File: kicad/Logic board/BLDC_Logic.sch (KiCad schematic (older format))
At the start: 21 parts

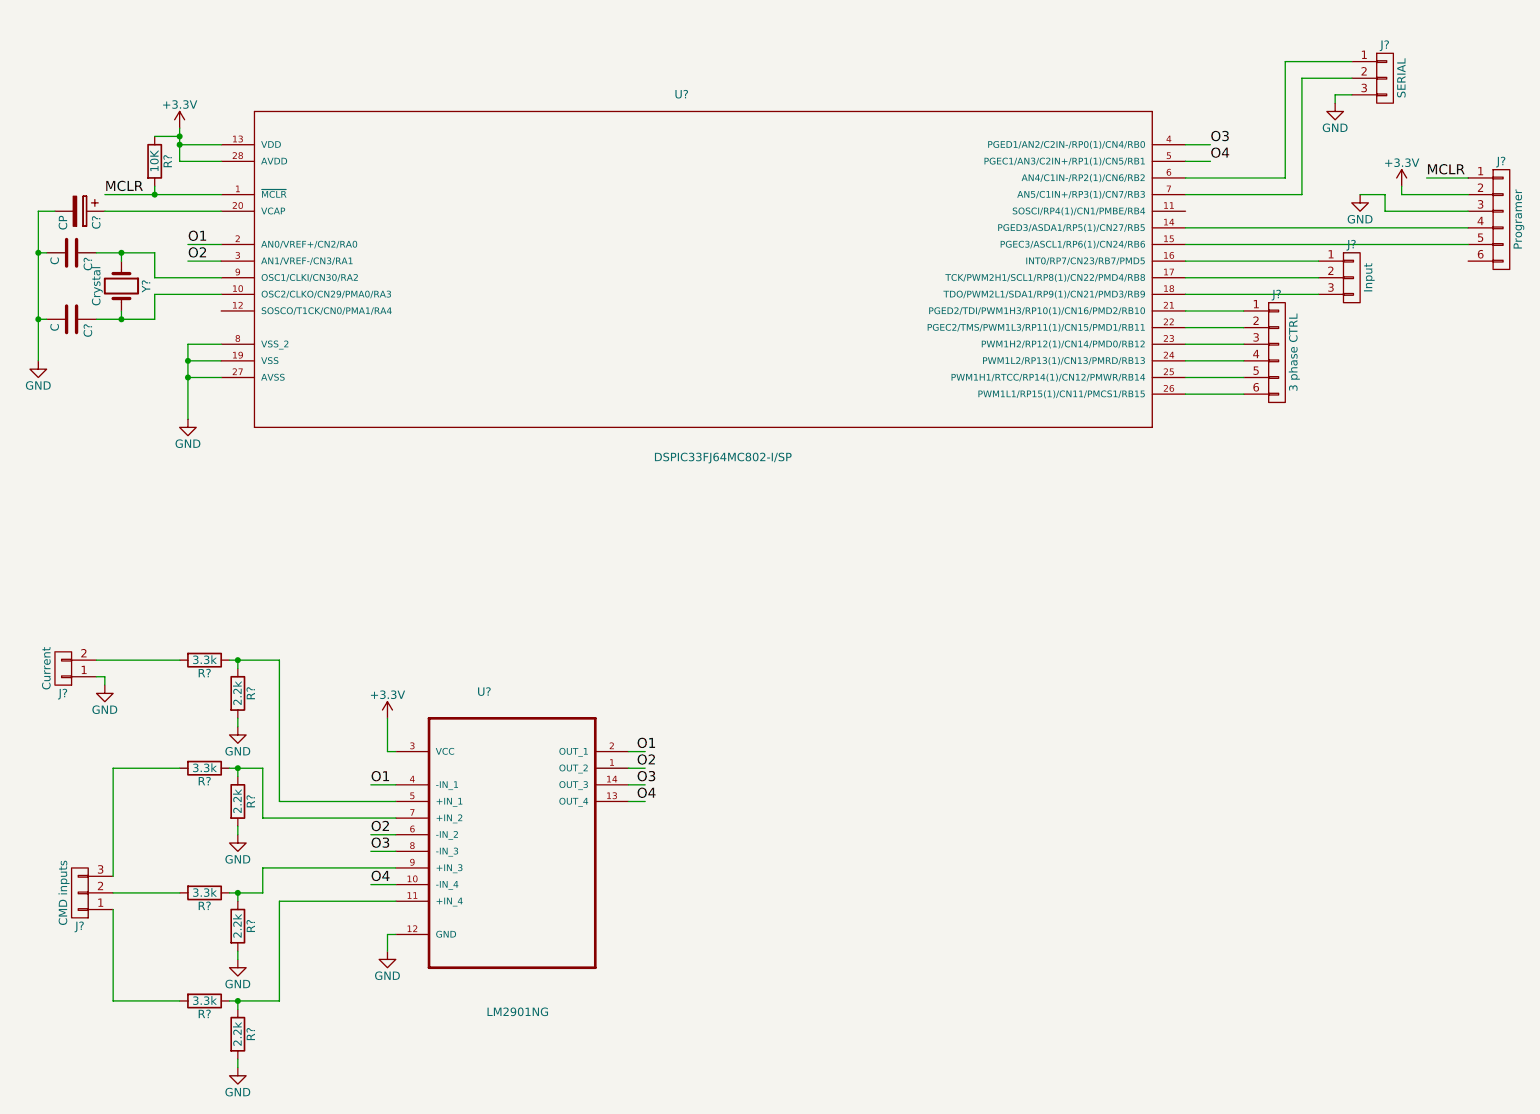
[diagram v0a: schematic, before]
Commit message: added MCLR Circuit
added MCLR circuit based on version 1 board
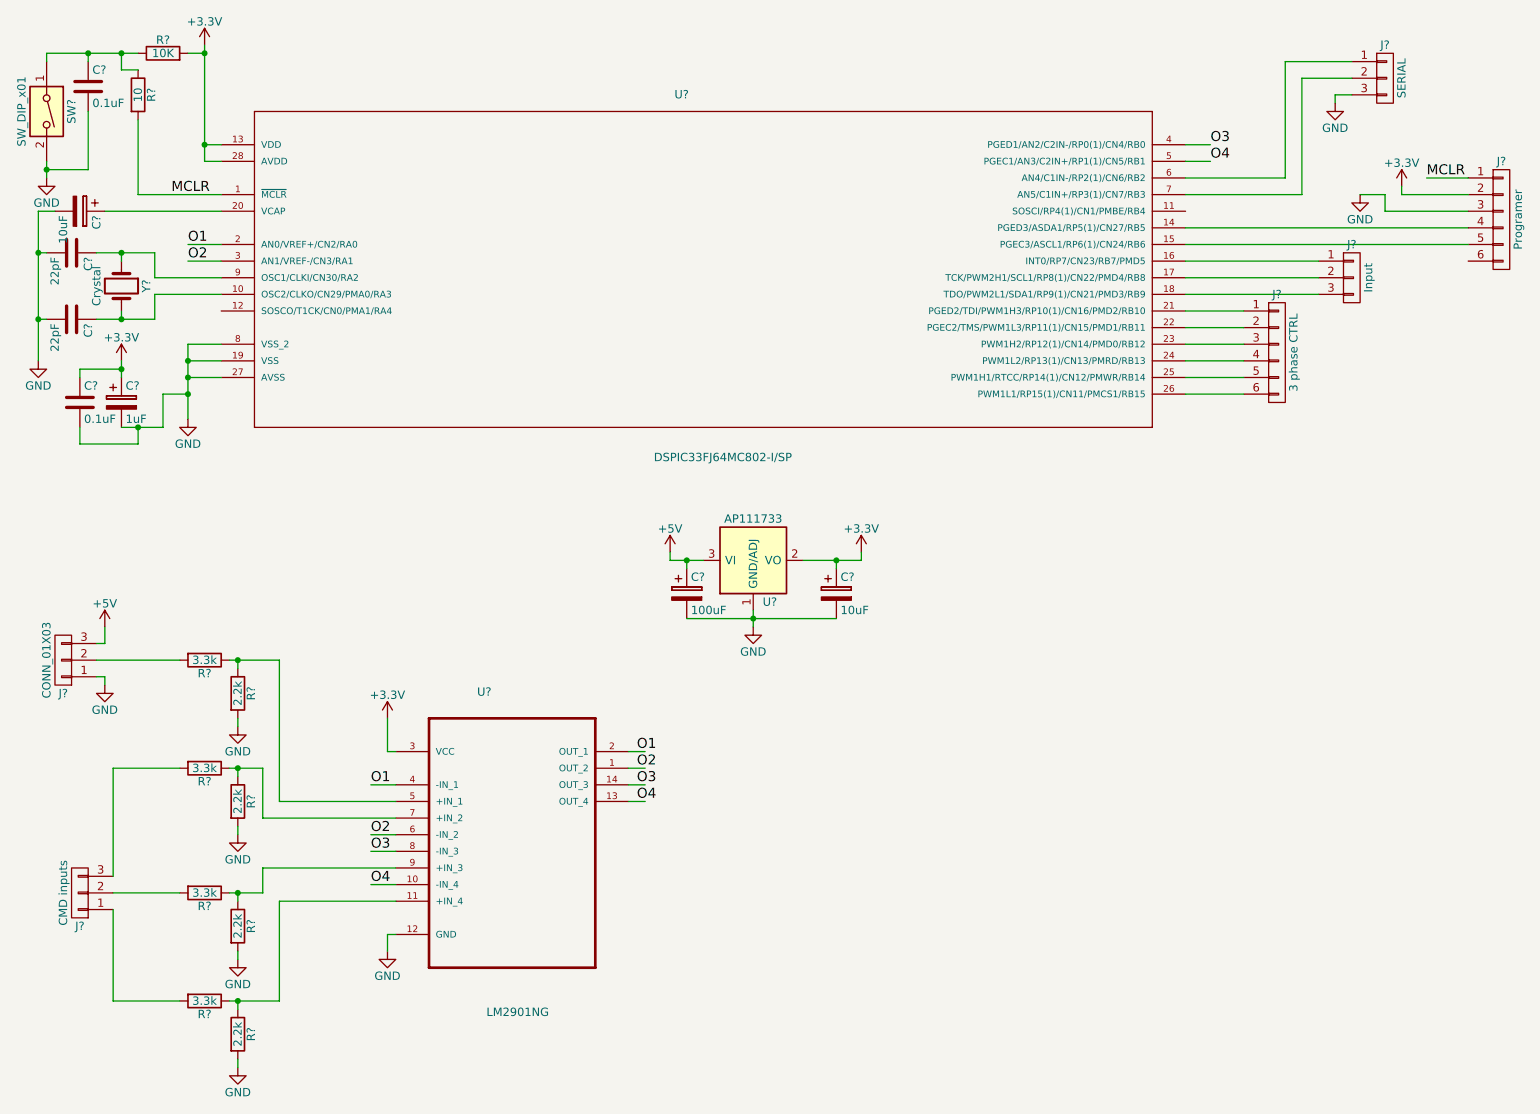
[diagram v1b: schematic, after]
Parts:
- removed J?: Current, symbol CONN_01X02
- added C?: 100uF, symbol CP
- added C?: 10uF, symbol CP
- added C?: 1uF, symbol CP
- added C? (x2): 0.1uF, symbol C
- added J?: CONN_01X03, symbol CONN_01X03
- added R?: 10, symbol R
- added SW?: SW_DIP_x01, symbol SW_DIP_x01
- added U?: AP111733, TO_SOT_Packages_SMD:SOT-223, symbol AP111733
- C?: value CP -> 10uF
- C? (x2): value C -> 22pF
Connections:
- net labels added: +5V
- wire segments 92 -> 119
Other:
- moved on the sheet: R?

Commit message: finished schmatic beggining layout
finished the schmatic of Logic board, layout is incomplete
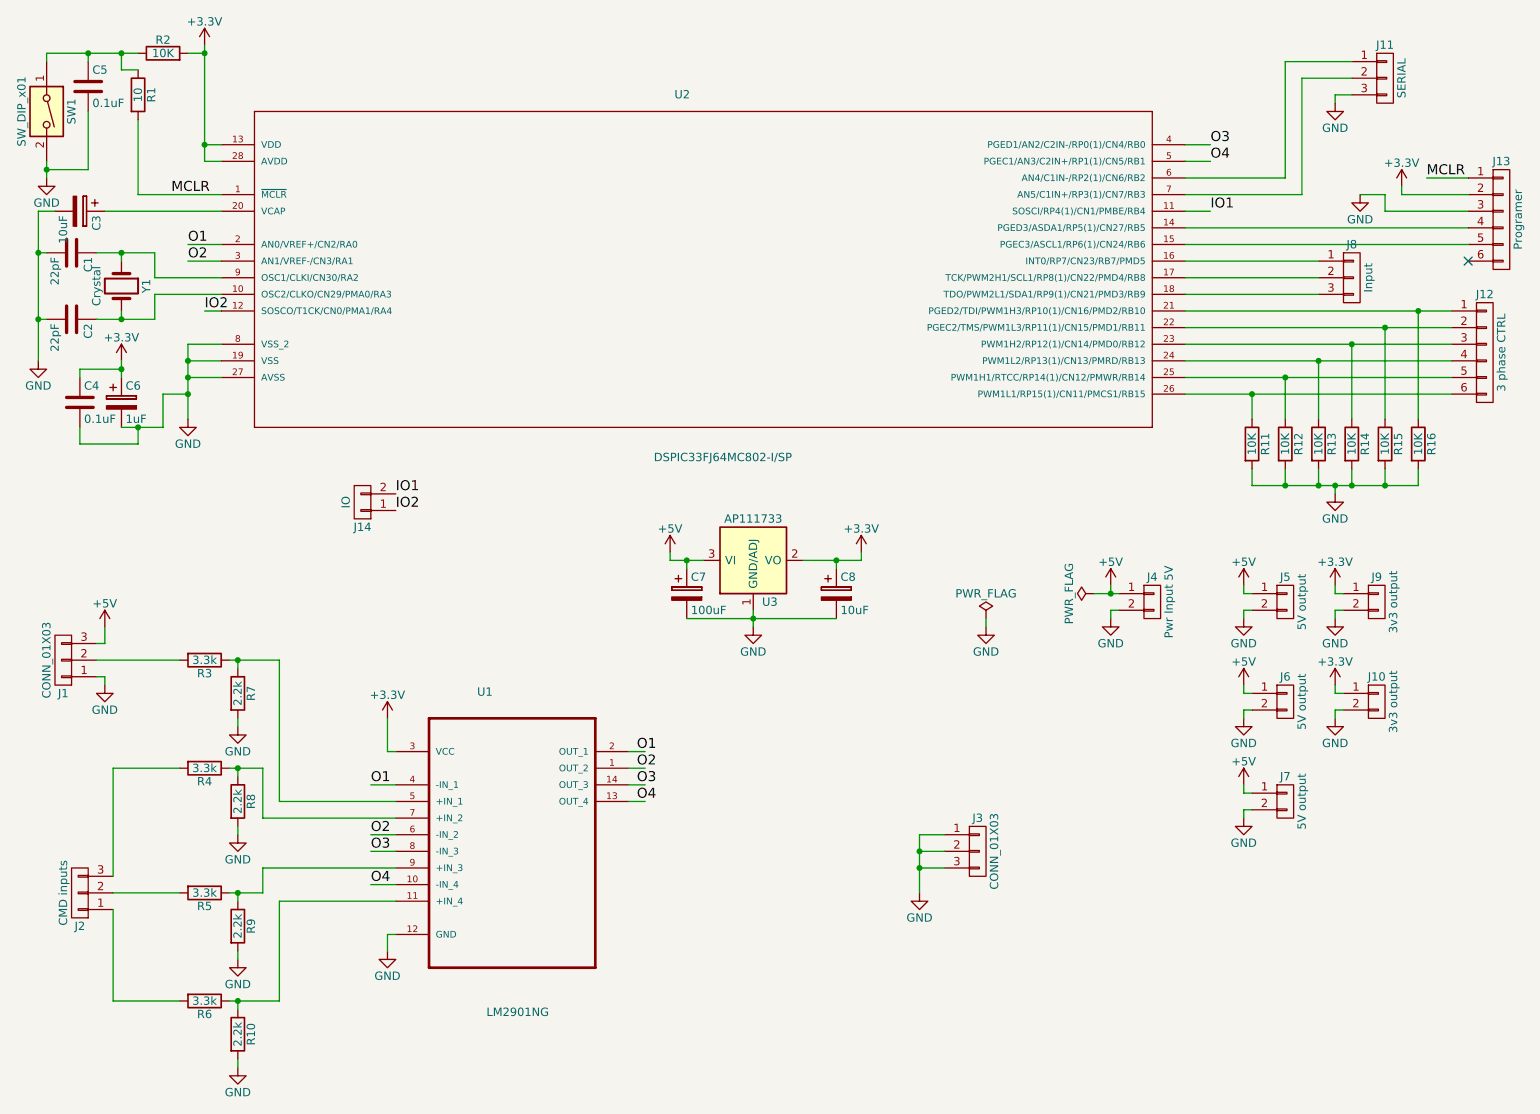
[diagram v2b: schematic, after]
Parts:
- added J10, J9: 3v3 output, Pin_Headers:Pin_Header_Straight_1x02_Pitch2.54mm, symbol CONN_01X02
- added J14: IO, Pin_Headers:Pin_Header_Straight_1x02_Pitch2.54mm, symbol CONN_01X02
- added J3: CONN_01X03, Pin_Headers:Pin_Header_Straight_1x03_Pitch2.54mm, symbol CONN_01X03
- added J4: Pwr Input 5V, Pin_Headers:Pin_Header_Straight_1x02_Pitch2.54mm, symbol CONN_01X02
- added J5, J6, J7: 5V output, Pin_Headers:Pin_Header_Straight_1x02_Pitch2.54mm, symbol CONN_01X02
- added R11, R12, R13, R14, R15, R16: 10K, Resistors_THT:R_Axial_DIN0207_L6.3mm_D2.5mm_P15.24mm_Horizontal, symbol R
- C1, C2: renamed from C?; footprint (none) -> Capacitors_THT:C_Disc_D3.0mm_W1.6mm_P2.50mm
- C3: renamed from C?; footprint (none) -> Capacitors_THT:CP_Radial_D4.0mm_P1.50mm
- C4, C5: renamed from C?; footprint (none) -> Capacitors_THT:C_Disc_D3.0mm_W2.0mm_P2.50mm
- C6, C8: renamed from C?; footprint (none) -> Capacitors_THT:CP_Radial_D4.0mm_P2.00mm
- C7: renamed from C?; footprint (none) -> Capacitors_THT:CP_Radial_D6.3mm_P2.50mm
- J1, J11, J2, J8: renamed from J?; footprint (none) -> Pin_Headers:Pin_Header_Straight_1x03_Pitch2.54mm
- J12, J13: renamed from J?; footprint (none) -> Pin_Headers:Pin_Header_Straight_1x06_Pitch2.54mm
- R1, R10, R2, R3, R4, R5, R6, R7, R8, R9: renamed from R?; footprint (none) -> Resistors_THT:R_Axial_DIN0207_L6.3mm_D2.5mm_P15.24mm_Horizontal
- SW1: renamed from SW?; footprint (none) -> Buttons_Switches_THT:SW_DIP_x1_W7.62mm_Slide_LowProfile
- U1: renamed from U?; footprint DIP254P762X469-14 -> Housings_DIP:DIP-14_W7.62mm
- U2: renamed from U?; footprint DIP254P762X508-28 -> DSPIC33FJ64MC802-I_SP:DIP254P762X508-28
- U3: renamed from U?; footprint TO_SOT_Packages_SMD:SOT-223 -> TO_SOT_Packages_THT:TO-220_Vertical
- Y1: renamed from Y?; footprint (none) -> Crystals:Crystal_HC49-U_Vertical
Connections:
- net labels added: IO1, IO2
- wire segments 119 -> 164
- no-connect marks 0 -> 1
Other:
- moved on the sheet: J12

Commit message: Finished PCB switched 3ph board connector
completed the PCB layout of the board, changed from a 6 pole connect to
an 8 pole to intergrate 6 pwm signals and 5 volt power into one
connector, replacing the sperate 2 pole power connector. ( mountiong
holes are still needed
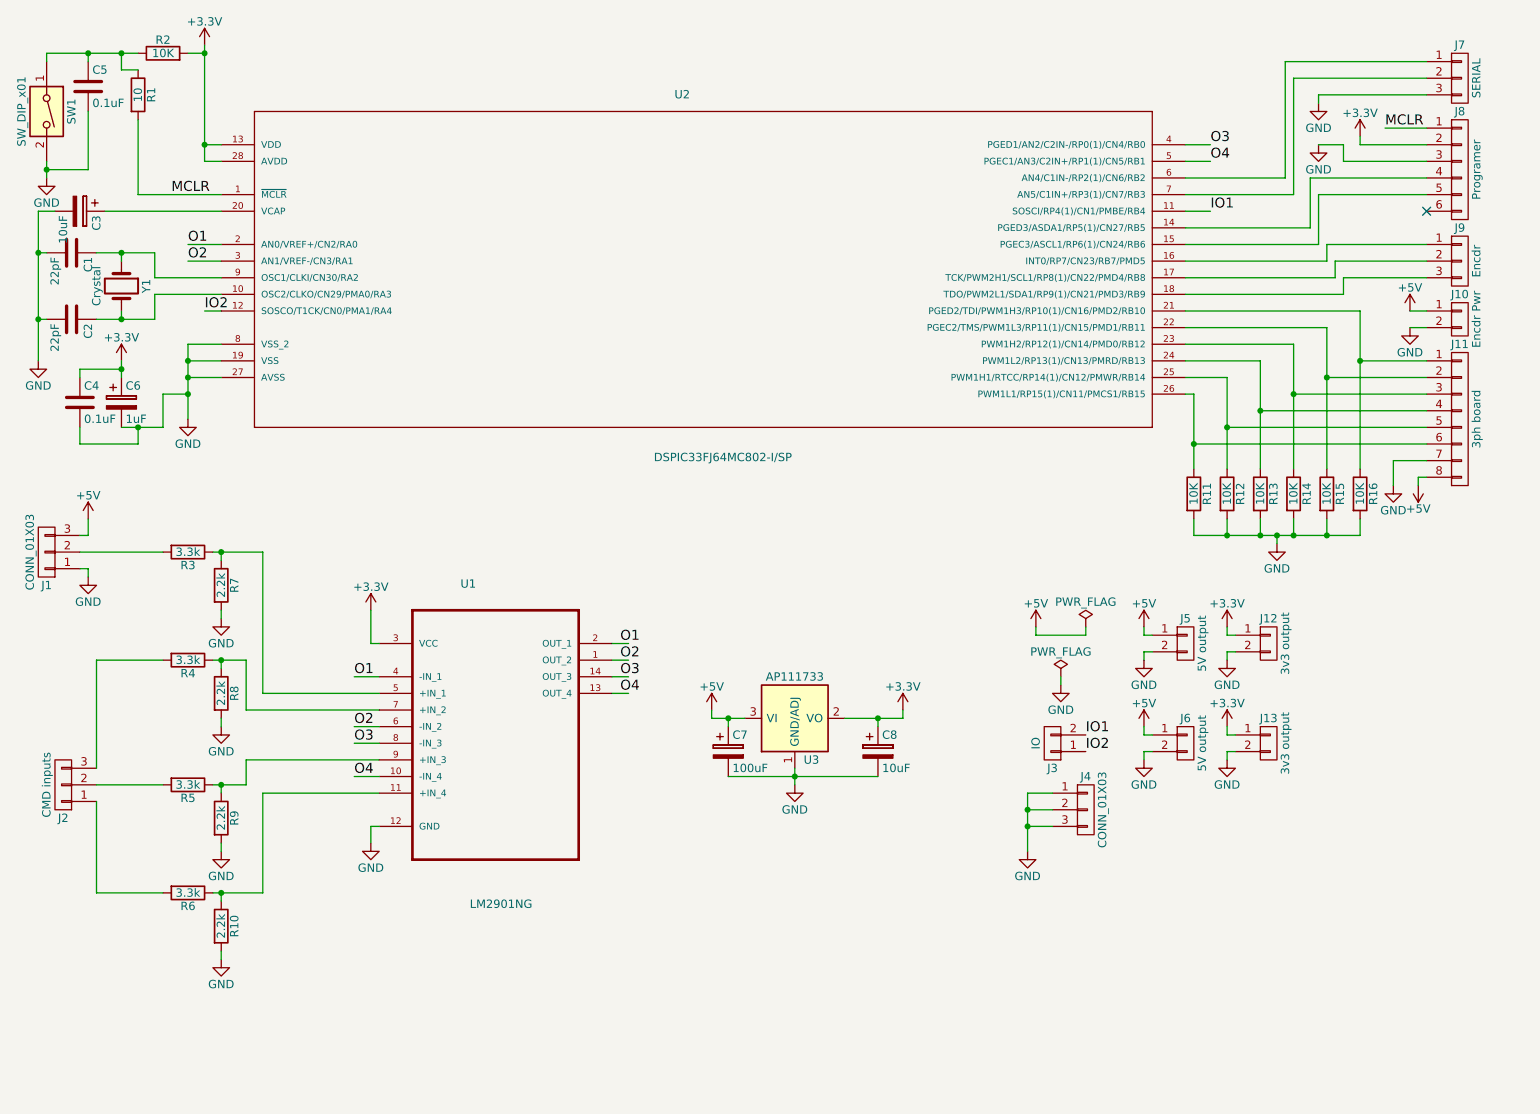
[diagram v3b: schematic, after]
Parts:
- removed J12: 3 phase CTRL, Pin_Headers:Pin_Header_Straight_1x06_Pitch2.54mm, symbol CONN_01X06
- removed J4: Pwr Input 5V, Pin_Headers:Pin_Header_Straight_1x02_Pitch2.54mm, symbol CONN_01X02
- added J11: 3ph board, Pin_Headers:Pin_Header_Straight_1x08_Pitch2.54mm, symbol CONN_01X08
- J10: renamed from J5; value 5V output -> Encdr Pwr
- J9: renamed from J8; value Input -> Encdr
- R1, R10, R11, R12, R13, R14, R15, R16, R2, R3, R4, R5, R6, R7, R8, R9: footprint Resistors_THT:R_Axial_DIN0207_L6.3mm_D2.5mm_P15.24mm_Horizontal -> Resistors_THT:R_Axial_DIN0204_L3.6mm_D1.6mm_P7.62mm_Horizontal
- SW1: footprint Buttons_Switches_THT:SW_DIP_x1_W7.62mm_Slide_LowProfile -> Buttons_Switches_THT:SW_PUSH-12mm
- renumbered J9 to J12, J10 to J13, J14 to J3, J3 to J4, J6 to J5, J7 to J6, J11 to J7, J13 to J8
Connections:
- net +5V: now also J11.8 (P8)
- net GND: now also J11.7 (P7)
- net at R16.1, U2.21 (PGED2/TDI/PWM1H3/RP10(1)/CN16/PMD2/RB10): now also J11.1 (P1)
- net at R15.1, U2.22 (PGEC2/TMS/PWM1L3/RP11(1)/CN15/PMD1/RB11): now also J11.2 (P2)
- net at R14.1, U2.23 (PWM1H2/RP12(1)/CN14/PMD0/RB12): now also J11.3 (P3)
- net at R13.1, U2.24 (PWM1L2/RP13(1)/CN13/PMRD/RB13): now also J11.4 (P4)
- net at R12.1, U2.25 (PWM1H1/RTCC/RP14(1)/CN12/PMWR/RB14): now also J11.5 (P5)
- net at R11.1, U2.26 (PWM1L1/RP15(1)/CN11/PMCS1/RB15): now also J11.6 (P6)
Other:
- moved on the sheet: C7, C8, J1, J10, J12, J13, J2, J3, J4, J5, J6, J7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

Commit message: changed the botton to better fit components. thickened traces for easier PCB fabrication. did some minor rerouting for smaller current loops.
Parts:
- SW1: footprint Buttons_Switches_THT:SW_PUSH-12mm -> Buttons_Switches_THT:SW_PUSH_6mm
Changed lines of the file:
@@
 F 0 "SW1" H 750 1550 50  0000 C CNN
 F 1 "SW_DIP_x01" H 750 1250 50  0000 C CNN
-F 2 "Buttons_Switches_THT:SW_PUSH-12mm" H 750 1400 50  0001 C CNN
+F 2 "Buttons_Switches_THT:SW_PUSH_6mm" H 750 1400 50  0001 C CNN
 F 3 "" H 750 1400 50  0001 C CNN
 	1    750  1400
